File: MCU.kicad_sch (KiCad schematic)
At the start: 1 part, among them U2 STM32L432KCUx

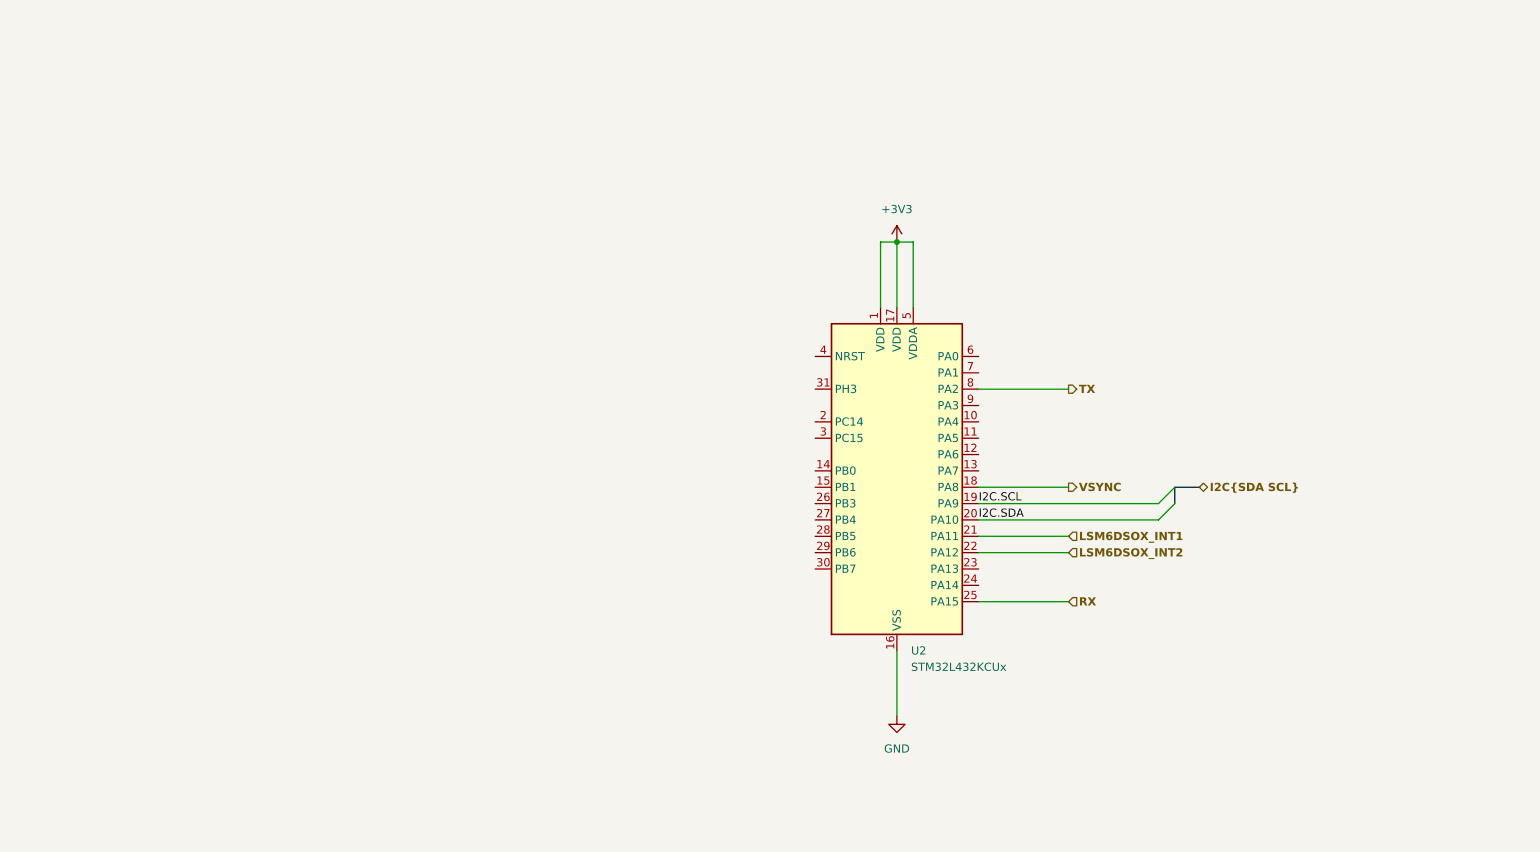
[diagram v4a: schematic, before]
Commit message: Completed schematic for MCU section
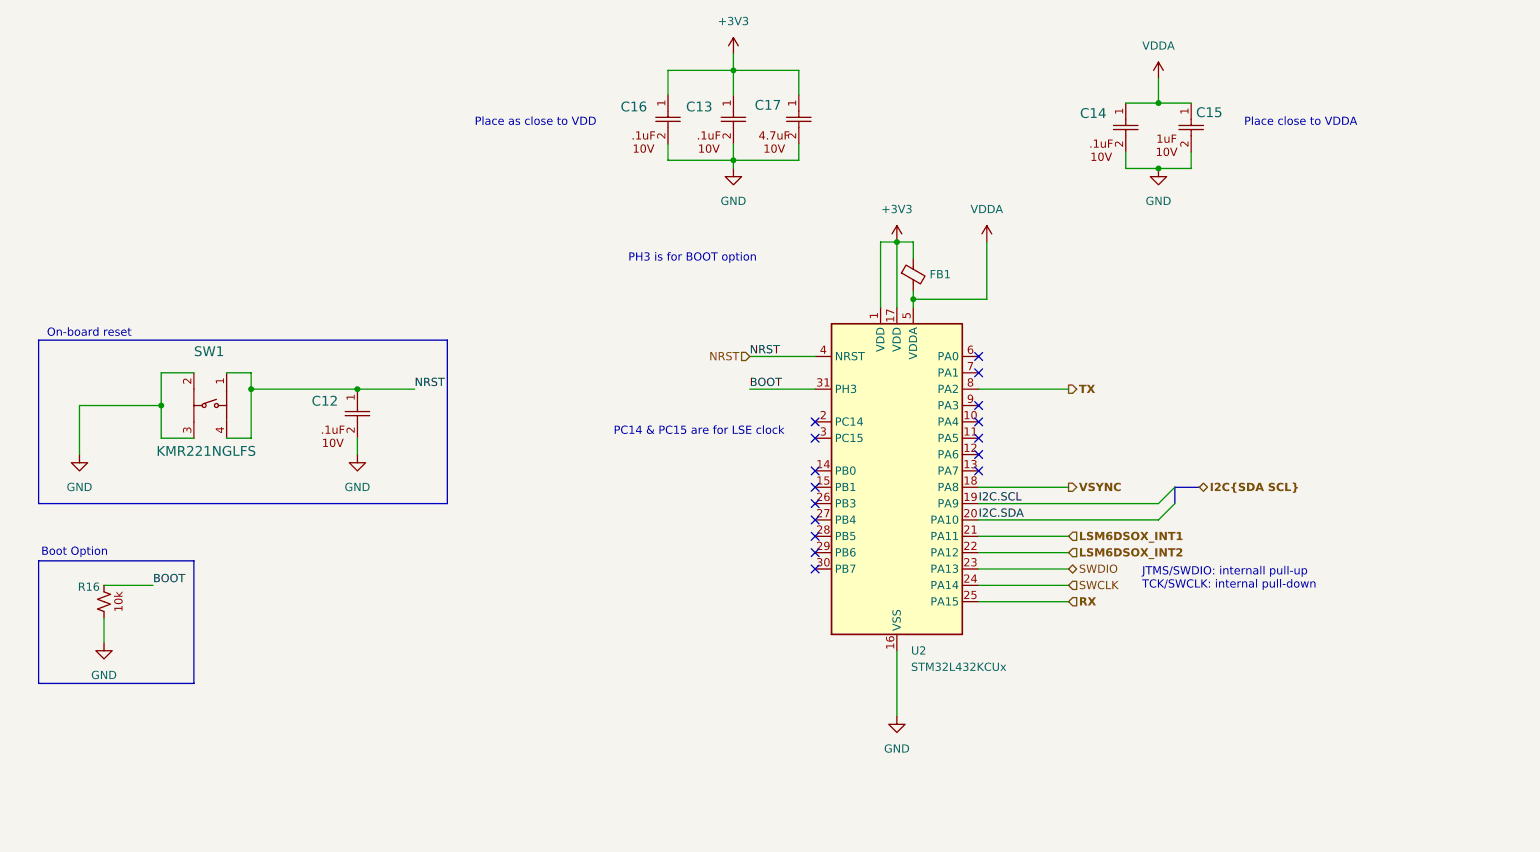
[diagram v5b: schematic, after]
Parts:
- added C12, C13, C14, C16: CC0402KRX7R6BB104, Hourglass_footprint_library:YAG_CC0402_YAG, symbol Hourglass_symbol_library:CC0402KRX7R6BB104
- added C15: GRM155Z71A105KE01D, Hourglass_footprint_library:CAP_GRM155Z_MUR, symbol Hourglass_symbol_library:GRM155Z71A105KE01D
- added C17: GRM21BR71A475KE51L, Hourglass_footprint_library:GRM21BR71A475KE51L, symbol Hourglass_symbol_library:GRM21BR71A475KE51L
- added FB1: FerriteBead_Small, Hourglass_footprint_library:FB_0603_1608Metric, symbol Hourglass_symbol_library:FerriteBead_Small
- added R16: RMCF0805FT10K0, Hourglass_footprint_library:RMCF0805FT10K0, symbol Hourglass_symbol_library:RMCF0805FT10K0
- added SW1: KMR221NGLFS, Hourglass_footprint_library:KMR221_CNK, symbol Hourglass_symbol_library:KMR221NGLFS
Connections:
- net +3V3: now also C13.1, C16.1, C17.1, FB1.1; no longer U2.5 (VDDA)
- net GND: now also C12.2, C13.2, C14.2, C15.2, C16.2, C17.2, R16., SW1.2, SW1.3
- net SWDIO: now reaches U2.23 (PA13)
- net SWCLK: now reaches U2.24 (PA14)
- net BOOT: now reaches U2.31 (PH3)
- net BOOT: now also R16.
- net NRST: now reaches U2.4 (NRST)
- net NRST: now also C12.1, SW1.1, SW1.4
- new net VDDA: C14.1, C15.1, FB1.2, U2.5 (VDDA)
- no-connect marks 0 -> 16
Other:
- note added: "Boot Option"
- note added: "JTMS/SWDIO: internall pull-up TCK/SWCLK: internal pull-down"
- note added: "On-board reset"
- note added: "PC14 & PC15 are for LSE clock"
- note added: "PH3 is for BOOT option"
- note added: "Place as close to VDD"
- note added: "Place close to VDDA"

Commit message: First complete schematic with TPs.
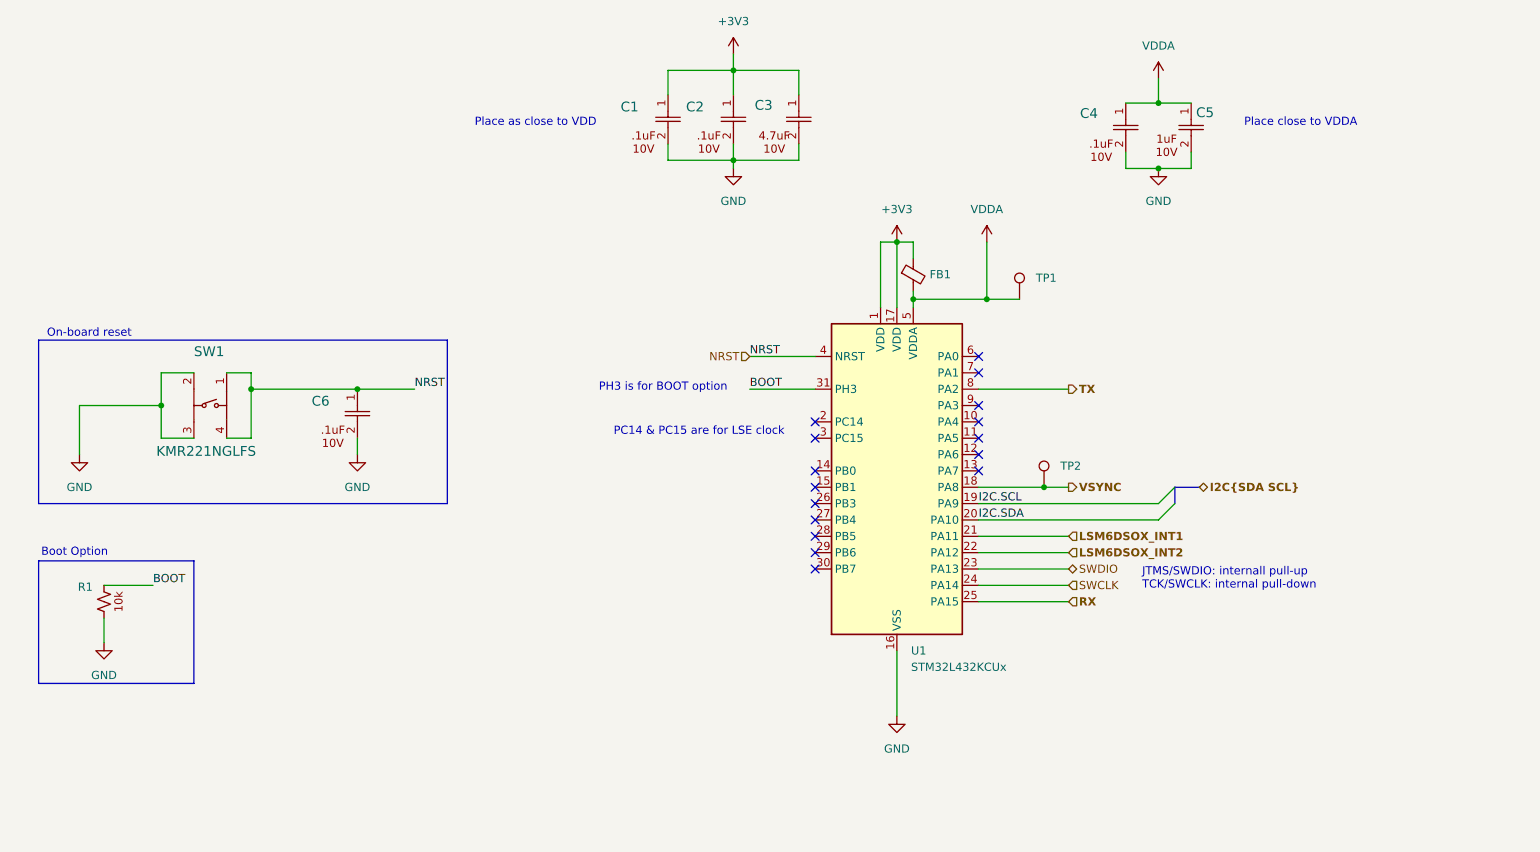
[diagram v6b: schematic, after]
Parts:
- added TP1, TP2: TestPoint, TestPoint:TestPoint_Pad_D1.0mm, symbol Connector:TestPoint
- renumbered C16 to C1, C13 to C2, C17 to C3, C14 to C4, C15 to C5, C12 to C6, R16 to R1, U2 to U1
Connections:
- net VDDA: now also TP1.1
- net VSYNC: now also TP2.1
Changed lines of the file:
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@@
 	(text "PH3 is for BOOT option "
 		(exclude_from_sim no)
-		(at 118.11 52.07 0)
+		(at 113.538 72.136 0)
 		(effects
 			(font
@@
 	)
 	(junction
+		(at 172.72 87.63)
+		(diameter 0)
+		(color 0 0 0 0)
+	)
+	(junction
 		(at 149.86 49.53)
 		(diameter 0)
@@
 	)
 	(junction
+		(at 163.83 58.42)
+		(diameter 0)
+		(color 0 0 0 0)
+	)
+	(junction
 		(at 190.5 27.94)
 		(diameter 0)
@@
 	(wire
 		(pts
-			(xy 176.53 97.79) (xy 162.56 97.79)
-		)
-		(stroke
-			(width 0)
-			(type default)
-		)
-	)
-	(wire
-		(pts
 			(xy 22.86 74.93) (xy 35.56 74.93)
 		)
@@
 	(wire
 		(pts
+			(xy 162.56 97.79) (xy 176.53 97.79)
+		)
+		(stroke
+			(width 0)
+			(type default)
+		)
+	)
+	(wire
+		(pts
 			(xy 49.53 72.39) (xy 66.04 72.39)
 		)
@@
 	(wire
 		(pts
+			(xy 163.83 58.42) (xy 168.91 58.42)
+		)
+		(stroke
+			(width 0)
+			(type default)
+		)
+	)
+	(wire
+		(pts
 			(xy 124.46 34.29) (xy 124.46 36.83)
 		)
@@
 	(wire
 		(pts
-			(xy 162.56 87.63) (xy 176.53 87.63)
+			(xy 162.56 87.63) (xy 172.72 87.63)
 		)
 		(stroke
@@
 		(pts
 			(xy 134.62 26.67) (xy 134.62 22.86)
+		)
+		(stroke
+			(width 0)
+			(type default)
+		)
+	)
+	(wire
+		(pts
+			(xy 172.72 87.63) (xy 176.53 87.63)
 		)
 		(stroke
@@
 		(dnp no)
 		(fields_autoplaced yes)
-		(property "Reference" "#PWR9"
+		(property "Reference" "#PWR010"
 			(at 149.86 129.54 0)
 			(effects
@@
 			(project ""
 				(path "/a75630d2-15a7-42bc-8ce0-7846cbd1da6b/c8d454a4-a64d-492c-9043-c9910b58426e"
-					(reference "#PWR9")
+					(reference "#PWR010")
 					(unit 1)
 				)
@@
 		(on_board yes)
 		(dnp no)
-		(property "Reference" "C12"
+		(property "Reference" "C6"
 			(at 58.928 74.2501 90)
 			(effects
@@
 			(project ""
 				(path "/a75630d2-15a7-42bc-8ce0-7846cbd1da6b/c8d454a4-a64d-492c-9043-c9910b58426e"
-					(reference "C12")
+					(reference "C6")
 					(unit 1)
 				)
@@
 		(dnp no)
 		(fields_autoplaced yes)
-		(property "Reference" "U2"
+		(property "Reference" "U1"
 			(at 152.0541 113.03 0)
 			(effects
@@
 			(project ""
 				(path "/a75630d2-15a7-42bc-8ce0-7846cbd1da6b/c8d454a4-a64d-492c-9043-c9910b58426e"
-					(reference "U2")
+					(reference "U1")
+					(unit 1)
+				)
+			)
+		)
+	)
+	(symbol
+		(lib_id "Connector:TestPoint")
+		(at 172.72 87.63 0)
+		(unit 1)
+		(exclude_from_sim no)
+		(in_bom yes)
+		(on_board yes)
+		(dnp no)
+		(fields_autoplaced yes)
+		(property "Reference" "TP2"
+			(at 175.26 84.3279 0)
+			(effects
+				(font
+					(size 1.27 1.27)
+				)
+				(justify left)
+			)
+		)
+		(property "Value" "TestPoint"
+			(at 175.26 85.5979 0)
+			(effects
+				(font
+					(size 1.27 1.27)
+				)
+				(justify left)
+				(hide yes)
+			)
+		)
+		(property "Footprint" "TestPoint:TestPoint_Pad_D1.0mm"
+			(at 177.8 87.63 0)
+			(effects
+				(font
+					(size 1.27 1.27)
+				)
+				(hide yes)
+			)
+		)
+		(property "Datasheet" "~"
+			(at 177.8 87.63 0)
+			(effects
+				(font
+					(size 1.27 1.27)
+				)
+				(hide yes)
+			)
+		)
+		(property "Description" "test point"
+			(at 172.72 87.63 0)
+			(effects
+				(font
+					(size 1.27 1.27)
+				)
+				(hide yes)
+			)
+		)
+		(pin "1"
+		)
+		(instances
+			(project ""
+				(path "/a75630d2-15a7-42bc-8ce0-7846cbd1da6b/c8d454a4-a64d-492c-9043-c9910b58426e"
+					(reference "TP2")
 					(unit 1)
 				)
@@
 		(on_board yes)
 		(dnp no)
-		(property "Reference" "C15"
+		(property "Reference" "C5"
 			(at 196.342 29.4191 90)
 			(effects
@@
 			(project ""
 				(path "/a75630d2-15a7-42bc-8ce0-7846cbd1da6b/c8d454a4-a64d-492c-9043-c9910b58426e"
-					(reference "C15")
+					(reference "C5")
 					(unit 1)
 				)
@@
 		(on_board yes)
 		(dnp no)
-		(property "Reference" "R16"
+		(property "Reference" "R1"
 			(at 22.606 103.1238 90)
 			(effects
@@
 			(project ""
 				(path "/a75630d2-15a7-42bc-8ce0-7846cbd1da6b/c8d454a4-a64d-492c-9043-c9910b58426e"
-					(reference "R16")
+					(reference "R1")
 					(unit 1)
 				)
@@
 		(dnp no)
 		(fields_autoplaced yes)
-		(property "Reference" "#PWR043"
+		(property "Reference" "#PWR03"
 			(at 124.46 44.45 0)
 			(effects
@@
 			(project "Hourglass_PCBA"
 				(path "/a75630d2-15a7-42bc-8ce0-7846cbd1da6b/c8d454a4-a64d-492c-9043-c9910b58426e"
-					(reference "#PWR043")
+					(reference "#PWR03")
 					(unit 1)
 				)
@@
 		(on_board yes)
 		(dnp no)
-		(property "Reference" "C17"
+		(property "Reference" "C3"
 			(at 127.762 28.2761 90)
 			(effects
@@
 			(project ""
 				(path "/a75630d2-15a7-42bc-8ce0-7846cbd1da6b/c8d454a4-a64d-492c-9043-c9910b58426e"
-					(reference "C17")
+					(reference "C3")
 					(unit 1)
 				)
@@
 		(dnp no)
 		(fields_autoplaced yes)
-		(property "Reference" "#PWR8"
+		(property "Reference" "#PWR05"
 			(at 149.86 53.34 0)
 			(effects
@@
 			(project ""
 				(path "/a75630d2-15a7-42bc-8ce0-7846cbd1da6b/c8d454a4-a64d-492c-9043-c9910b58426e"
-					(reference "#PWR8")
+					(reference "#PWR05")
 					(unit 1)
 				)
@@
 		(dnp no)
 		(fields_autoplaced yes)
-		(property "Reference" "#PWR041"
+		(property "Reference" "#PWR04"
 			(at 190.5 44.45 0)
 			(effects
@@
 			(project ""
 				(path "/a75630d2-15a7-42bc-8ce0-7846cbd1da6b/c8d454a4-a64d-492c-9043-c9910b58426e"
-					(reference "#PWR041")
+					(reference "#PWR04")
 					(unit 1)
 				)
@@
 		(dnp no)
 		(fields_autoplaced yes)
-		(property "Reference" "#PWR037"
+		(property "Reference" "#PWR08"
 			(at 66.04 88.9 0)
 			(effects
@@
 			(project ""
 				(path "/a75630d2-15a7-42bc-8ce0-7846cbd1da6b/c8d454a4-a64d-492c-9043-c9910b58426e"
-					(reference "#PWR037")
+					(reference "#PWR08")
 					(unit 1)
 				)
@@
 		(on_board yes)
 		(dnp no)
-		(property "Reference" "C13"
+		(property "Reference" "C2"
 			(at 117.094 28.5301 90)
 			(effects
@@
 			(project ""
 				(path "/a75630d2-15a7-42bc-8ce0-7846cbd1da6b/c8d454a4-a64d-492c-9043-c9910b58426e"
-					(reference "C13")
+					(reference "C2")
+					(unit 1)
+				)
+			)
+		)
+	)
+	(symbol
+		(lib_id "Connector:TestPoint")
+		(at 168.91 58.42 0)
+		(unit 1)
+		(exclude_from_sim no)
+		(in_bom yes)
+		(on_board yes)
+		(dnp no)
+		(fields_autoplaced yes)
+		(property "Reference" "TP1"
+			(at 171.45 55.1179 0)
+			(effects
+				(font
+					(size 1.27 1.27)
+				)
+				(justify left)
+			)
+		)
+		(property "Value" "TestPoint"
+			(at 171.45 56.3879 0)
+			(effects
+				(font
+					(size 1.27 1.27)
+				)
+				(justify left)
+				(hide yes)
+			)
+		)
+		(property "Footprint" "TestPoint:TestPoint_Pad_D1.0mm"
+			(at 173.99 58.42 0)
+			(effects
+				(font
+					(size 1.27 1.27)
+				)
+				(hide yes)
+			)
+		)
+		(property "Datasheet" "~"
+			(at 173.99 58.42 0)
+			(effects
+				(font
+					(size 1.27 1.27)
+				)
+				(hide yes)
+			)
+		)
+		(property "Description" "test point"
+			(at 168.91 58.42 0)
+			(effects
+				(font
+					(size 1.27 1.27)
+				)
+				(hide yes)
+			)
+		)
+		(pin "1"
+		)
+		(instances
+			(project "Hourglass_PCBA"
+				(path "/a75630d2-15a7-42bc-8ce0-7846cbd1da6b/c8d454a4-a64d-492c-9043-c9910b58426e"
+					(reference "TP1")
 					(unit 1)
 				)
@@
 		(on_board yes)
 		(dnp no)
-		(property "Reference" "#PWR040"
+		(property "Reference" "#PWR02"
 			(at 190.5 27.94 0)
 			(effects
@@
 			(project "Hourglass_PCBA"
 				(path "/a75630d2-15a7-42bc-8ce0-7846cbd1da6b/c8d454a4-a64d-492c-9043-c9910b58426e"
-					(reference "#PWR040")
+					(reference "#PWR02")
 					(unit 1)
 				)
@@
 		(dnp no)
 		(fields_autoplaced yes)
-		(property "Reference" "#PWR038"
+		(property "Reference" "#PWR07"
 			(at 22.86 88.9 0)
 			(effects
@@
 			(project ""
 				(path "/a75630d2-15a7-42bc-8ce0-7846cbd1da6b/c8d454a4-a64d-492c-9043-c9910b58426e"
-					(reference "#PWR038")
+					(reference "#PWR07")
 					(unit 1)
 				)
@@
 		(dnp no)
 		(fields_autoplaced yes)
-		(property "Reference" "#PWR042"
+		(property "Reference" "#PWR01"
 			(at 124.46 24.13 0)
 			(effects
@@
 			(project "Hourglass_PCBA"
 				(path "/a75630d2-15a7-42bc-8ce0-7846cbd1da6b/c8d454a4-a64d-492c-9043-c9910b58426e"
-					(reference "#PWR042")
+					(reference "#PWR01")
 					(unit 1)
 				)
@@
 		(dnp no)
 		(fields_autoplaced yes)
-		(property "Reference" "#PWR044"
+		(property "Reference" "#PWR09"
 			(at 26.67 118.11 0)
 			(effects
@@
 			(project ""
 				(path "/a75630d2-15a7-42bc-8ce0-7846cbd1da6b/c8d454a4-a64d-492c-9043-c9910b58426e"
-					(reference "#PWR044")
+					(reference "#PWR09")
 					(unit 1)
 				)
@@
 		(on_board yes)
 		(dnp no)
-		(property "Reference" "C14"
+		(property "Reference" "C4"
 			(at 178.308 29.5461 90)
 			(effects
@@
 			(project "Hourglass_PCBA"
 				(path "/a75630d2-15a7-42bc-8ce0-7846cbd1da6b/c8d454a4-a64d-492c-9043-c9910b58426e"
-					(reference "C14")
+					(reference "C4")
 					(unit 1)
 				)
@@
 		(on_board yes)
 		(dnp no)
-		(property "Reference" "C16"
+		(property "Reference" "C1"
 			(at 106.934 28.5301 90)
 			(effects
@@
 			(project "Hourglass_PCBA"
 				(path "/a75630d2-15a7-42bc-8ce0-7846cbd1da6b/c8d454a4-a64d-492c-9043-c9910b58426e"
-					(reference "C16")
+					(reference "C1")
 					(unit 1)
 				)
@@
 		(dnp no)
 		(fields_autoplaced yes)
-		(property "Reference" "#PWR039"
+		(property "Reference" "#PWR06"
 			(at 163.83 53.34 0)
 			(effects
@@
 			(project ""
 				(path "/a75630d2-15a7-42bc-8ce0-7846cbd1da6b/c8d454a4-a64d-492c-9043-c9910b58426e"
-					(reference "#PWR039")
+					(reference "#PWR06")
 					(unit 1)
 				)

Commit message: Addressed DRC warnings and errors.
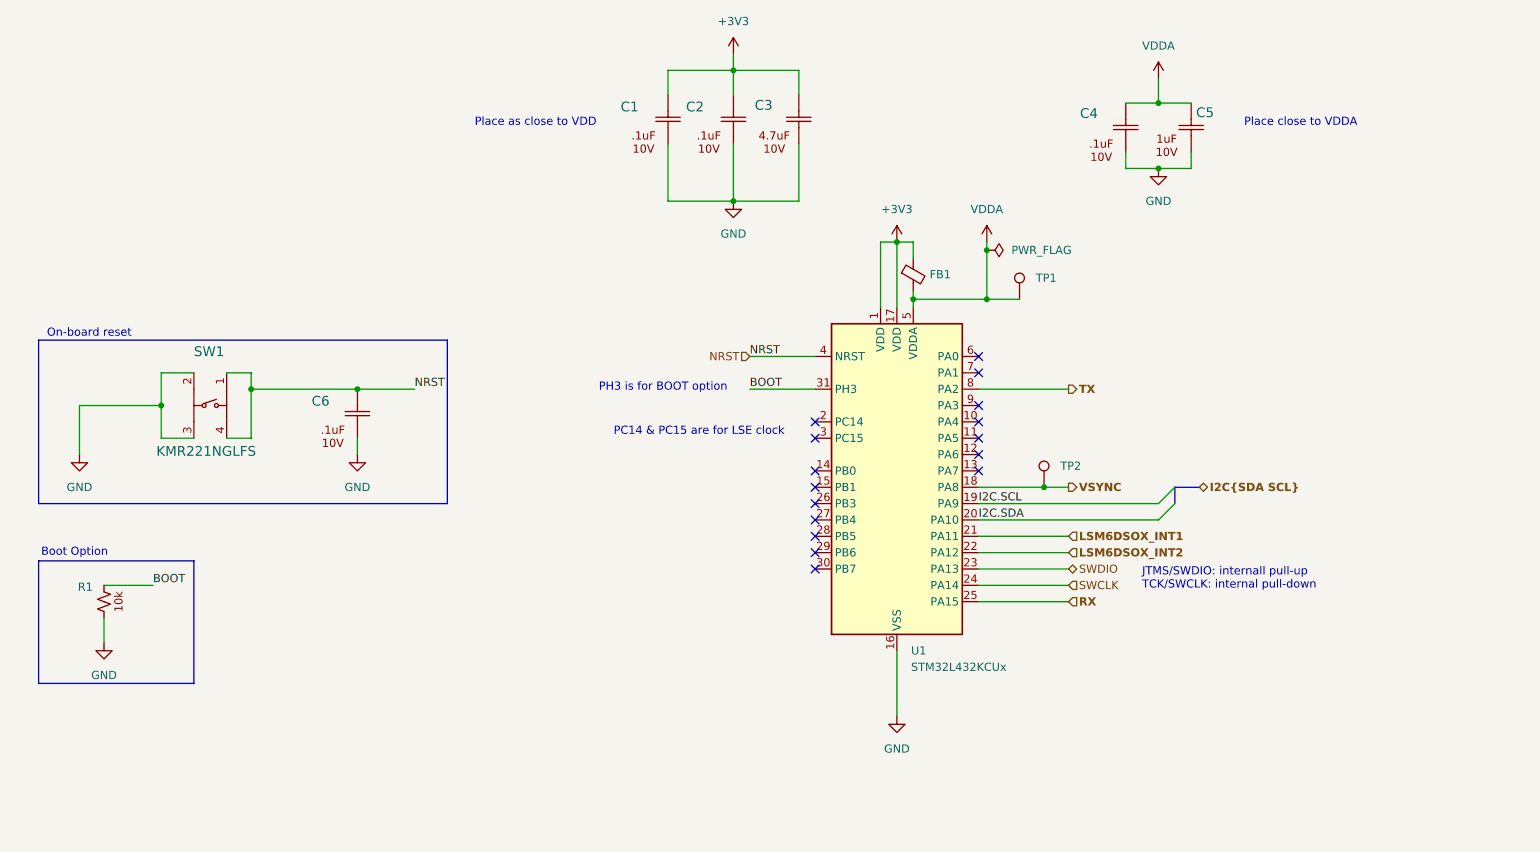
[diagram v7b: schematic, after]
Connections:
- net BOOT: now also R1.2; no longer R1.
- net GND: now also R1.1; no longer R1.
